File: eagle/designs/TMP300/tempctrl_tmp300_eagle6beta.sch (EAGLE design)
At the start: 22 parts, among them IC1 TMP300, Q1 NIF5002

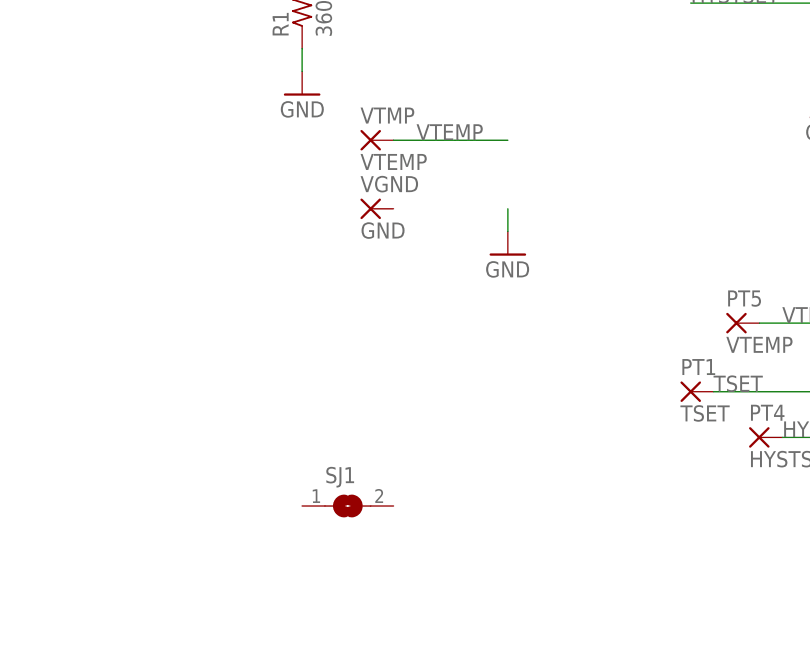
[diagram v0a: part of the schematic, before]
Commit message: Moved jumper into position and wired up ground connection.
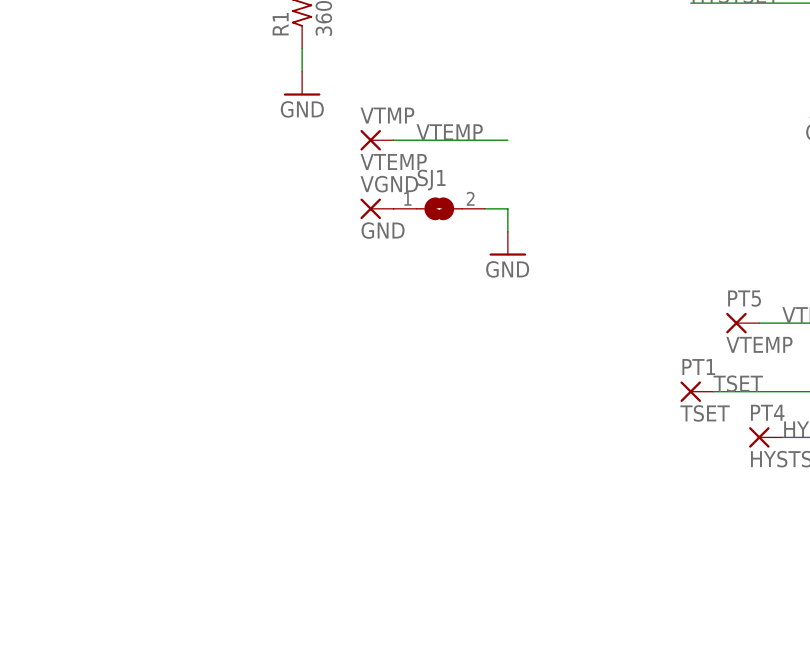
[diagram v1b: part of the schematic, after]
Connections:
- new net N$1: SJ1.1, VGND.P
- net GND: now also SJ1.2
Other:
- moved on the sheet: SJ1
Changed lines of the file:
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@@
 <instance part="P+4" gate="1" x="106.68" y="154.94"/>
 <instance part="VSS" gate="P" x="104.14" y="175.26" rot="R270"/>
-<instance part="SJ1" gate="1" x="53.34" y="88.9"/>
+<instance part="SJ1" gate="1" x="63.5" y="121.92"/>
 </instances>
 <busses>
@@
 <wire x1="71.12" y1="121.92" x2="71.12" y2="119.38" width="0.1524" layer="91"/>
 <pinref part="GND7" gate="1" pin="GND"/>
+<pinref part="SJ1" gate="1" pin="2"/>
+<wire x1="68.58" y1="121.92" x2="71.12" y2="121.92" width="0.1524" layer="91"/>
 </segment>
 <segment>
@@
 </segment>
 </net>
+<net name="N$1" class="0">
+<segment>
+<pinref part="VGND" gate="P" pin="P"/>
+<pinref part="SJ1" gate="1" pin="1"/>
+</segment>
+</net>
